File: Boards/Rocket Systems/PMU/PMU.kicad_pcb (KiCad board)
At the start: 4 copper layers, 138 x 62 mm, 155 parts, among them IC1 LM4040DIZ-4.1_NOPB, IC2 LM4040DIZ-4.1_NOPB, IC3 LM4040DIZ-4.1_NOPB, IC4 LS1205EFD33, IC5 LM358BIPWR, IC6 LM358BIPWR, IC7 LM358BIPWR, J1 172298-1104, J10 1723163304, J2 XT30UPB-F, J3 XT30UPB-F, J4 XT30UPB-F, J5 XT30UPB-F, J6 1723163304, J8 XT30UPB-F, J9 1723163304, K3 G3VM-31DR_TR05_, K4 G3VM-31DR_TR05_, K5 G3VM-31DR_TR05_, Q1 NPN, Q2 PMOS, Q3 NPN, Q4 NPN, Q5 NPN, Q6 NPN, Q7 NPN, Q8 NPN, U10 ST1L05APU33R, U11 NCR321UX, U12 NCR321UX, U13 NCR321UX, U29 NCV8114ASN165T1G, U3 STPS15L45CB, U30 MCP6002-E/MS, U4 STPS15L45CB, U7 NJD35N04T4G, U8 NJD35N04T4G, U9 NJD35N04T4G

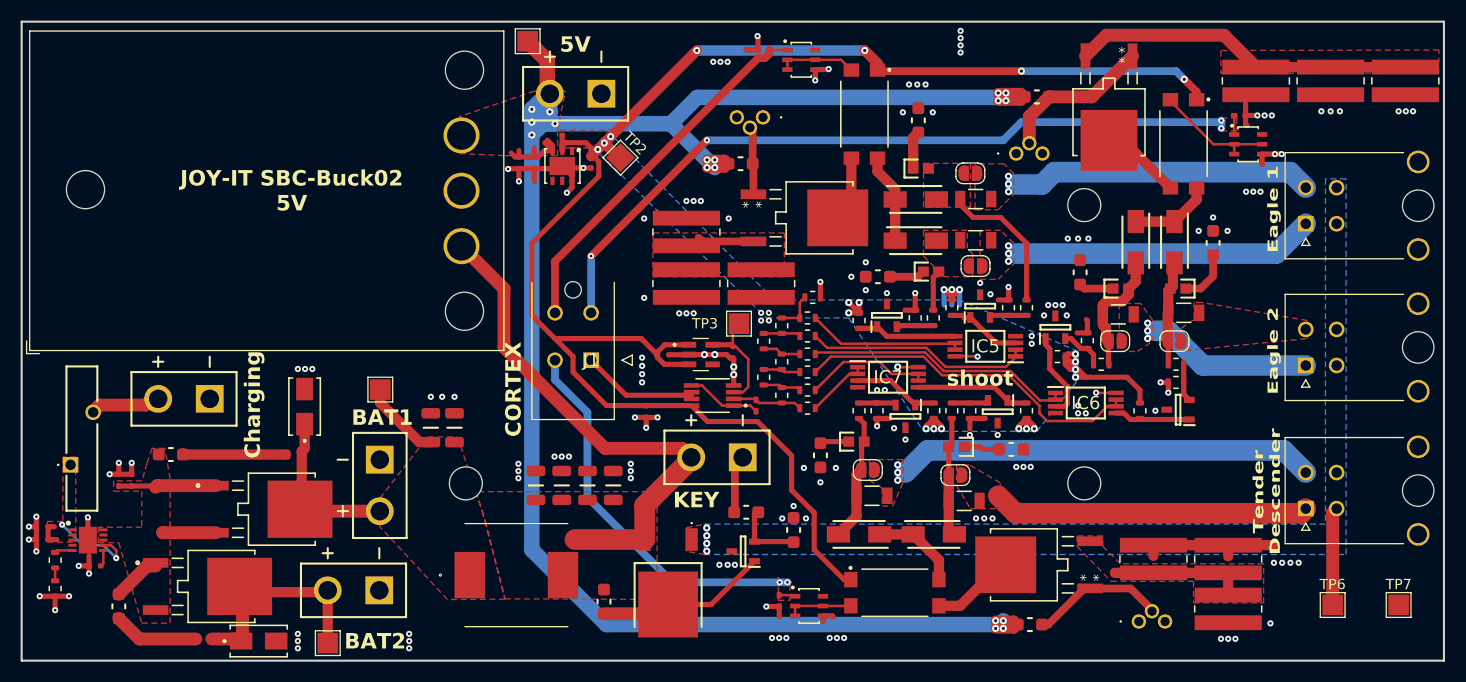
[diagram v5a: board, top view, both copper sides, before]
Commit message: PMU
Troca de DC DC e adição de algum labeling que faltava
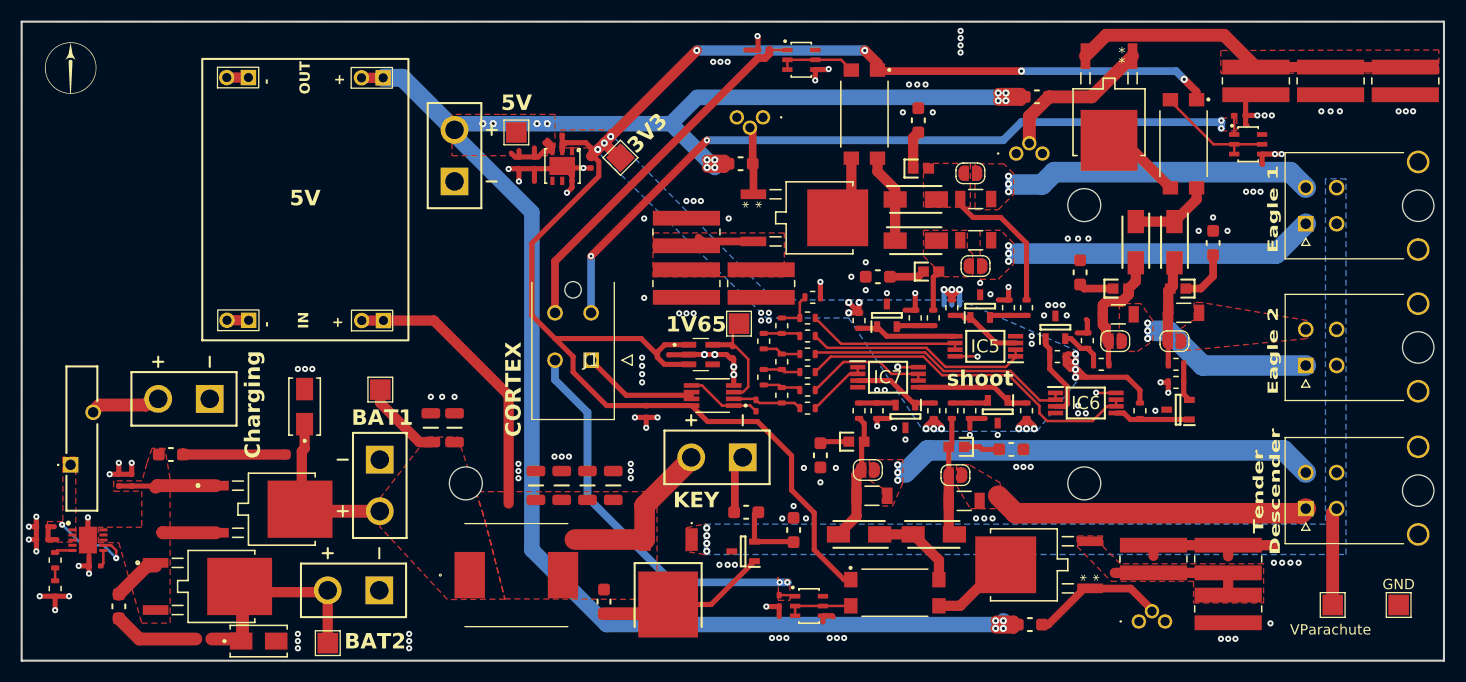
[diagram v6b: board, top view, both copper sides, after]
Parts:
- removed PC1: JOY-IT SBC-Buck02, Converter_DCDC:Converter_DCDC_XP_POWER-ITXxxxxSA_THT
- added G***: LOGO, LogoPST:LogoPST, F.Cu at (96.2, 49.5)
- added U2: ~, DCDCModule:DCDC_Module, F.Cu at (118.6, 62.2)
- moved J8 16.6 mm to (133.5, 60.5), turned to 0 degrees
- moved TP1 8.92 mm to (139.5, 55.8)
- renumbered TP7 to GND, TP6 to VParachute
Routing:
- net VDC: track 104.9 -> 97.8 mm
- net GND: track 90.5 -> 94.7 mm
- net +5V: track 188.4 -> 187.1 mm, vias 17 -> 16
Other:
- board text added: "1V65"
- board text added: "3V3"
- board text removed: "JOY-IT SBC-Buck02 5V"

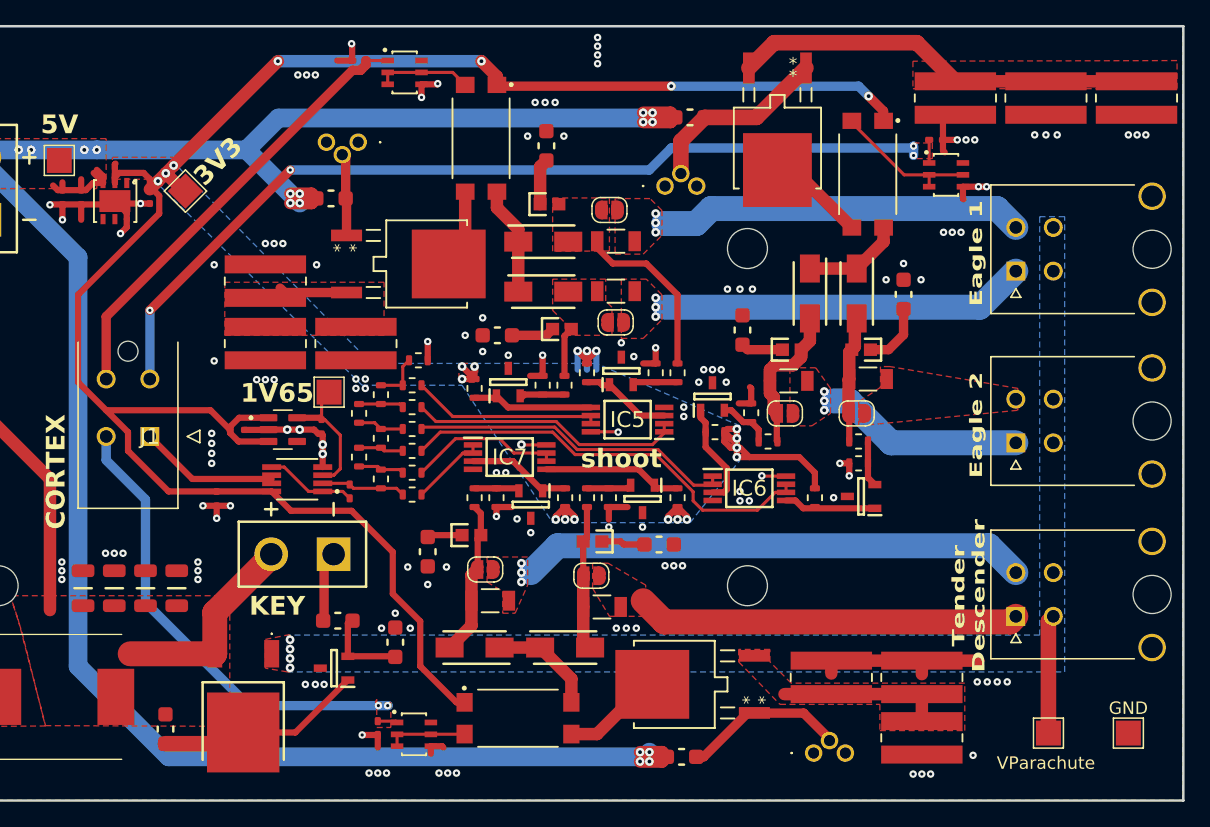
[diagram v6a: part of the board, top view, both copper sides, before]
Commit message: PMU
Mudança do Input do ADC para evitar saturação do opamp
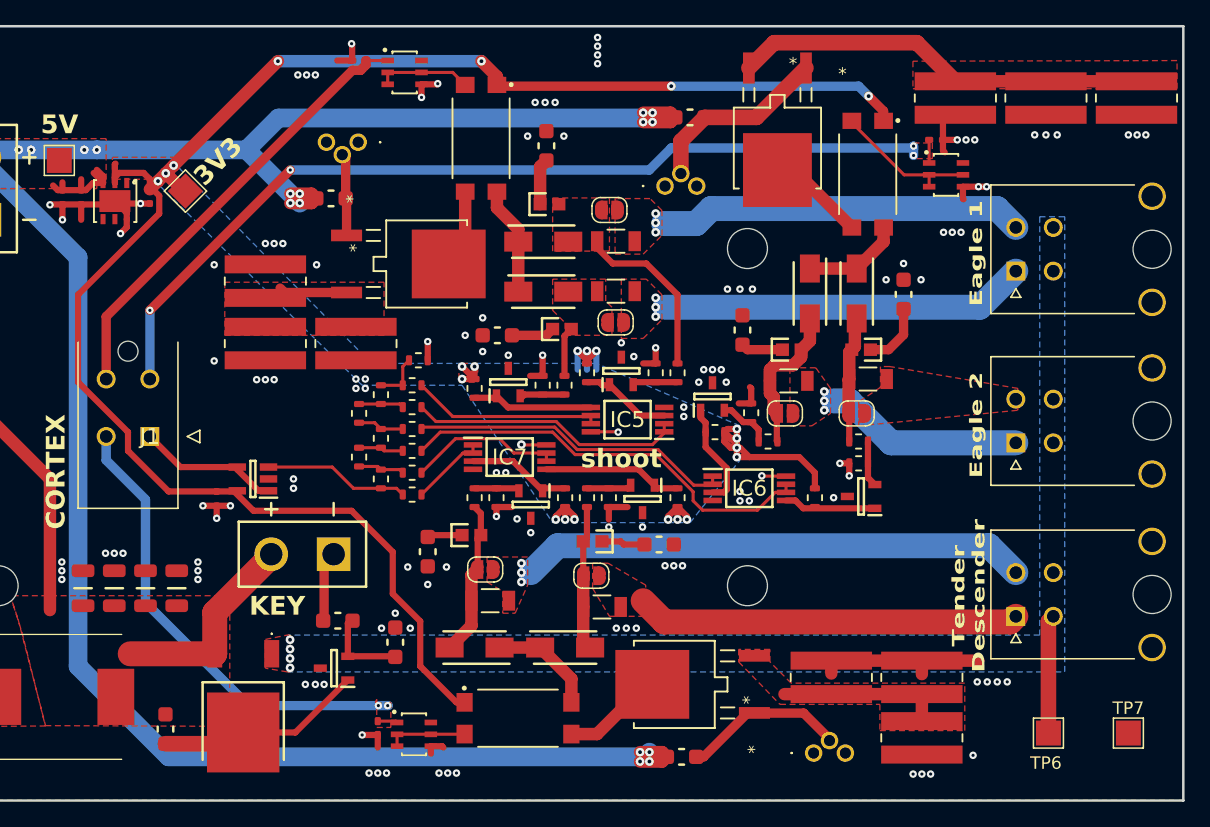
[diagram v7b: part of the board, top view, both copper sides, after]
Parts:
- removed C92: 100n, Capacitor-0402:Capacitor_0402
- removed C93: 10n, Capacitor-0402:Capacitor_0402
- removed R76: 1k, Resistor-0402:RES_0402
- removed TP3: TestPoint, TestPoint:TestPoint_Pad_2.0x2.0mm
- removed U29: NCV8114ASN165T1G, NCV8114ASN165T1G:SOT95P275X120-5N
- removed U30: MCP6002-E/MS, MCP6002-E-MS:MSOP8_MC_MCH
- added IC8: MCP6001T-I_OT, MCP6001-IOT:SOT95P270X145-5N, F.Cu at (155.0, 81.2)
- renumbered VParachute to TP6, GND to TP7
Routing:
- net +3.3V: track 193.2 -> 175.4 mm
- net +1.65V: track 10.8 -> 0.00 mm
- net GND: track 94.7 -> 85.6 mm, vias 156 -> 150
- net /BUFF IN: track 7.29 -> 0.00 mm
- net Net-(IC8-VIN+): track 6.78 -> 11.7 mm
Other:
- board text removed: "1V65"
